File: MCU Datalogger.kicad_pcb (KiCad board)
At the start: 2 copper layers, 61 x 40.6 mm, 30 parts, among them J1 Conn_01x04_Pin, J2 Conn_01x04_Pin, J3 Conn_01x09_Pin, J4 Conn_02x03_Odd_Even, U1 24LC1025, U2 24LC1025, U3 DS1337S_, U4 ATMEGA328P-AU, Y1 16MHz, Y2 32.768 KHz

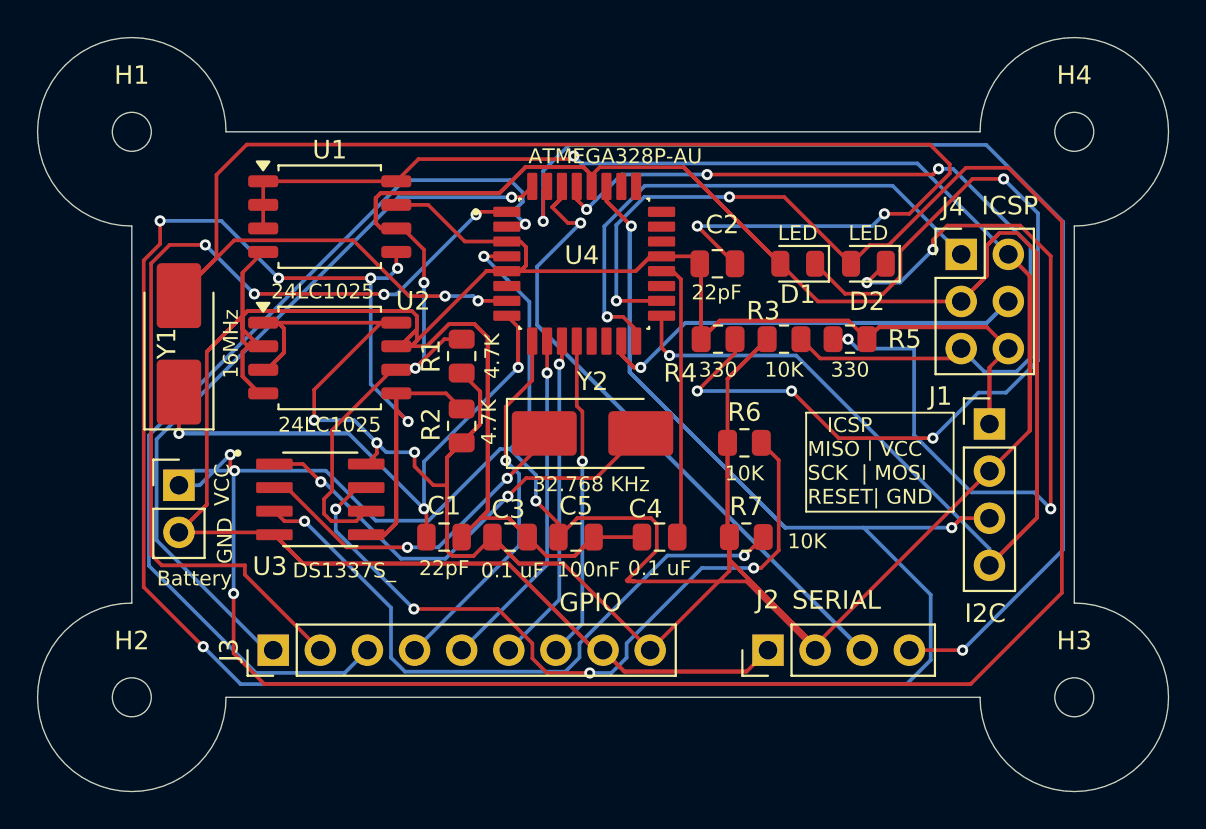
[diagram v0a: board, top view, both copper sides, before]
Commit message: fixed 2layer PCB
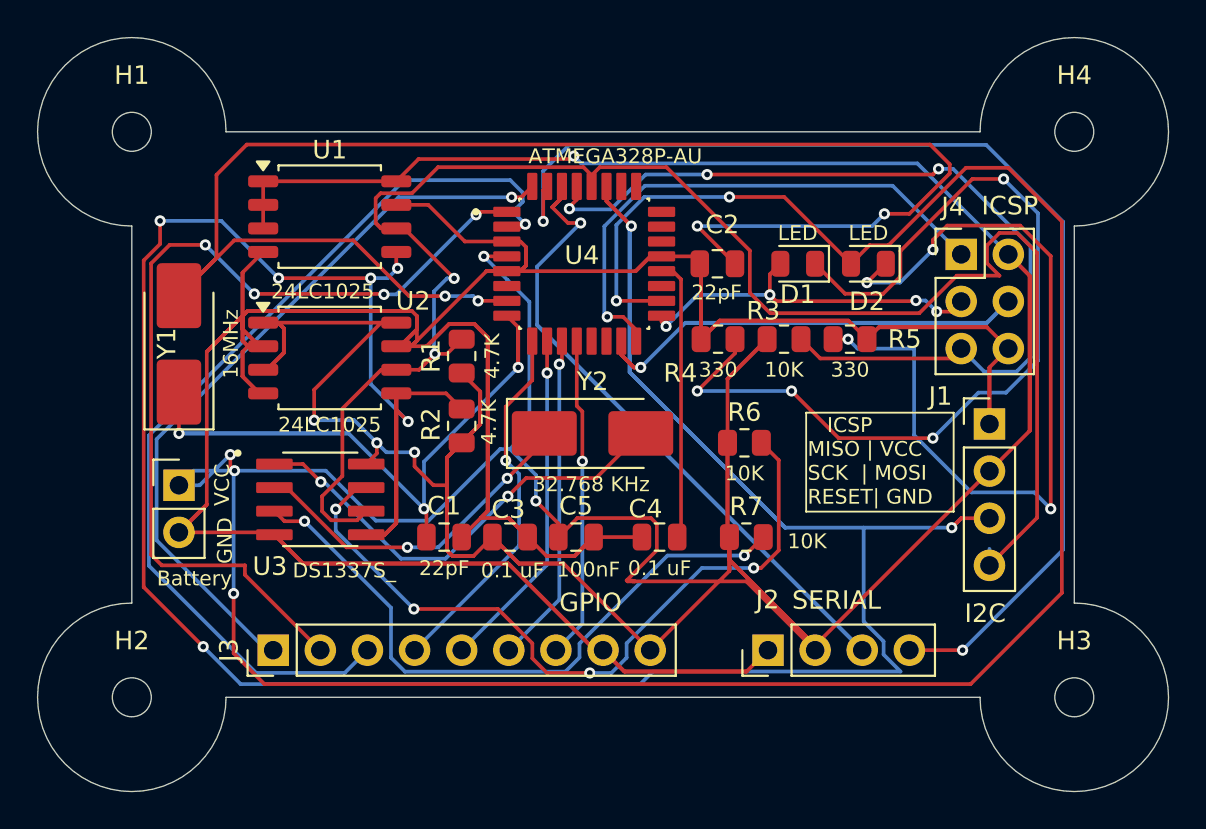
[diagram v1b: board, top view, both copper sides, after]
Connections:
- J1 pad 4: /SCK -> /SCL
- R1 pad 2: /SCK -> /SCL
- U1 pad 6: /SCK -> /SCL
- U2 pad 6: /SCK -> /SCL
- U3 pad 6: /SCK -> /SCL
- U4 pad 28: /SCK -> /SCL
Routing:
- net /SCK: track 157.5 -> 19.8 mm, vias 3 -> 4
- net /SCL: track 0.00 -> 94.2 mm, vias 0 -> 2
- net /SDA: track 185.1 -> 183.2 mm
- net /RESET: track 47.9 -> 48.7 mm
